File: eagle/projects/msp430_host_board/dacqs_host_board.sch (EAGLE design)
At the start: 114 parts, among them J1 MOL-SL-4-RA, J10 MOL-SL-3-V, J13 JST-PH-2TH-RA, J14 USB_MICROB_RECPT, J16 MOL-SL-2-RA, J17 CLM-112-02-L-D-IMU-MOUNT_IMU, J18 MOLSL-7-RA, J2 MOL-SL-4-RA, J3 MOL-SL-4-RA, J4 MOL-SL-4-RA, J5 MOL-SL-5-RA, J6 MOL-SL-3-V, J7 MOL-SL-5-V, J8 MOL-SL-3-RA, J9 MOL-SL-4-RA, U1 MSP430FR4994, U2 MSP430FR4994, U3 PCT2075D,118, U4 MS560702BA03-50, U5 TPS61240DRVR, U6 LP5907_DBV_5, U7 MCP73831T, U8 INA219AIDCNR, U9 STD12NF06LT4, Y1 32.768kHz, Y2 4MHz, Y3 32.768kHz, Y4 4MHz

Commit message: Bunch of small changes
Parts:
- added NC1, NC2, NC3, NC4: NC, daqcs_host:NO_CONNECT
- added TP1, TP10, TP11, TP12, TP13, TP14, TP15, TP16, TP17, TP18, TP19, TP2, TP20, TP21, TP22, TP23, TP24, TP25, TP26, TP27, TP28, TP29, TP3, TP30, TP31, TP32, TP33, TP34, TP4, TP5, TP6, TP7, TP8, TP9: (no value), daqcs_host:TEST_POINT_TP10R_SMD_10R_SMD
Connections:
- net N$47 renamed LED_BLUE_5V
- new net N$1: NC1.NC, R12.2
- new net N$2: NC3.NC, U$1.DAT1
- new net N$3: NC4.NC, U$1.DAT2
- net +5V: now also TP34.TP
- net ACT_CURRENT_IN: now also TP23.TP
- net ACT_SPEED_IN: now also TP22.TP
- net COMMS_MISO: now also TP15.TP
- net COMMS_MOSI: now also TP16.TP
- net COMMS_SCLK: now also TP14.TP
- net COMMS_SS: now also TP13.TP
- net CURRENT_PWM_OUT: now also TP19.TP
- net CUTDOWN_EN: now also TP17.TP
- net DIR_MOTOR_OUT: now also TP21.TP
- net EN_MOTOR_OUT: now also TP20.TP
- net IMU_MISO: now also TP30.TP
- net IMU_MOSI: now also TP33.TP
- net IMU_SCLK: now also TP32.TP
- net IMU_SS: now also TP31.TP
- net N$30: now also NC2.NC
- net RST_PI_1: now also TP3.TP
- net RST_PI_2: now also TP6.TP
- net RST_PI_3: now also TP9.TP
- net RST_PI_4: now also TP12.TP
- net SENSE_SCL_1: now also TP27.TP, TP29.TP
- net SENSE_SCL_2: now also TP25.TP
- net SENSE_SDA_1: now also TP26.TP, TP28.TP
- net SENSE_SDA_2: now also TP24.TP
- net SPEED_PWM_OUT: now also TP18.TP
- net UART_1_RX: now also TP2.TP
- net UART_1_TX: now also TP1.TP
- net UART_2_RX: now also TP5.TP
- net UART_2_TX: now also TP4.TP
- net UART_3_RX: now also TP8.TP
- net UART_3_TX: now also TP7.TP
- net UART_4_RX: now also TP11.TP
- net UART_4_TX: now also TP10.TP
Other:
- moved on the sheet: C27, J11

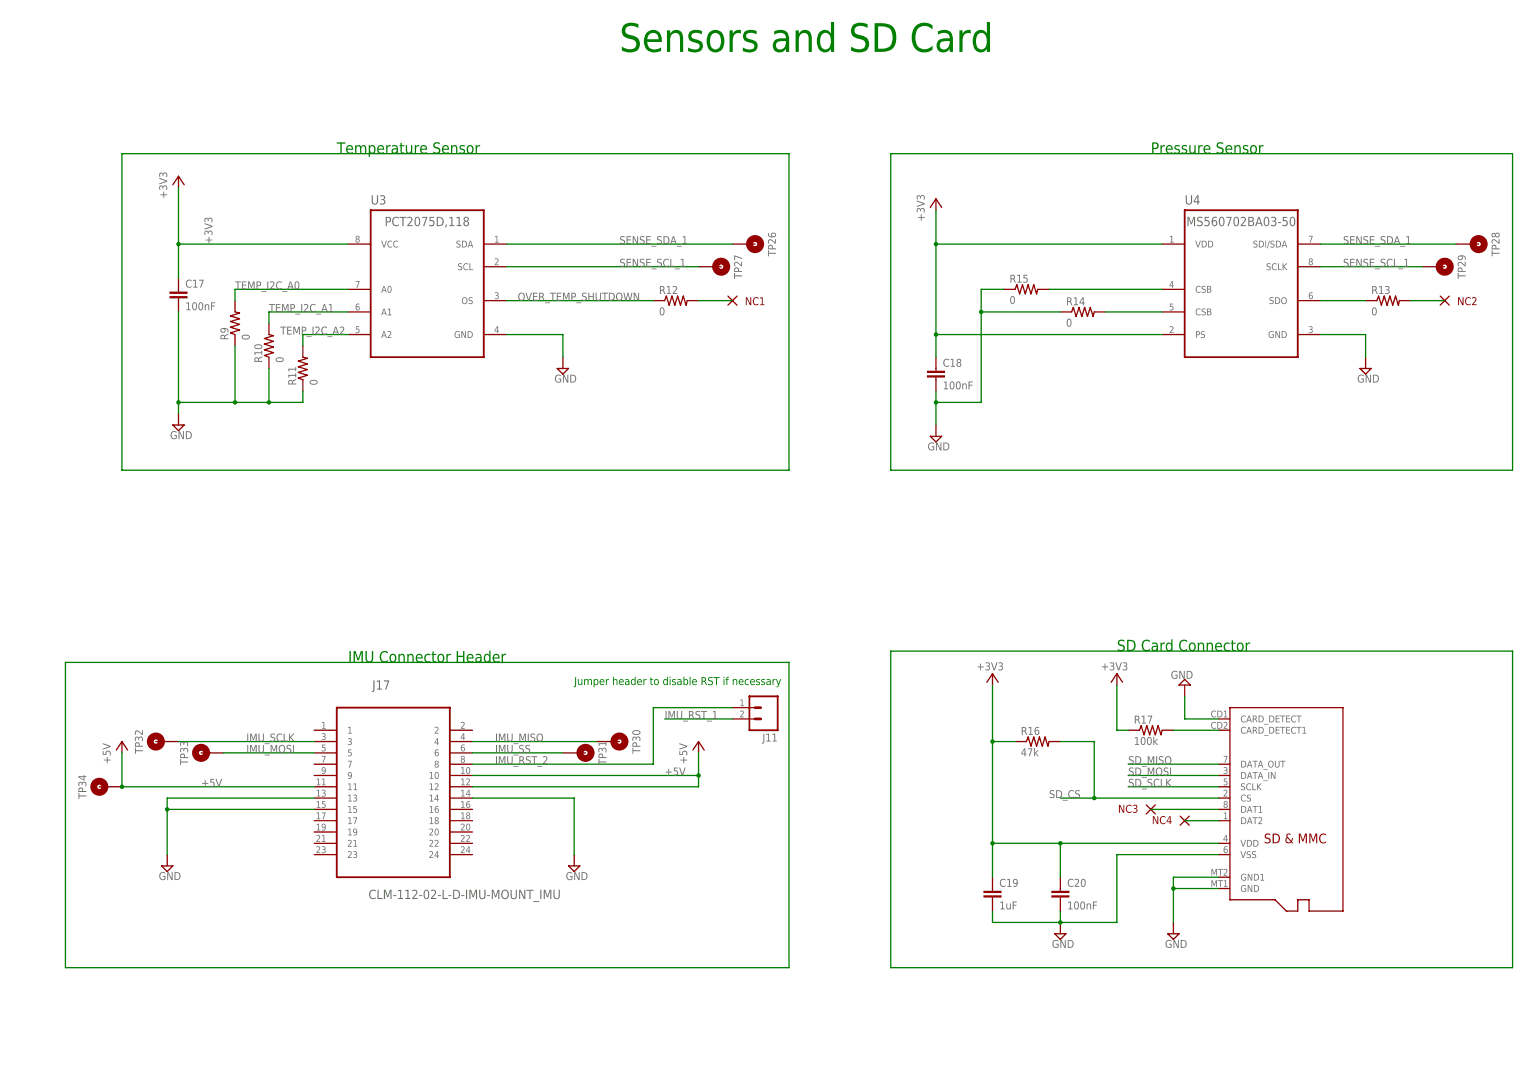
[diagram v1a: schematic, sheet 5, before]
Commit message: Added additional IMU with I2C interface
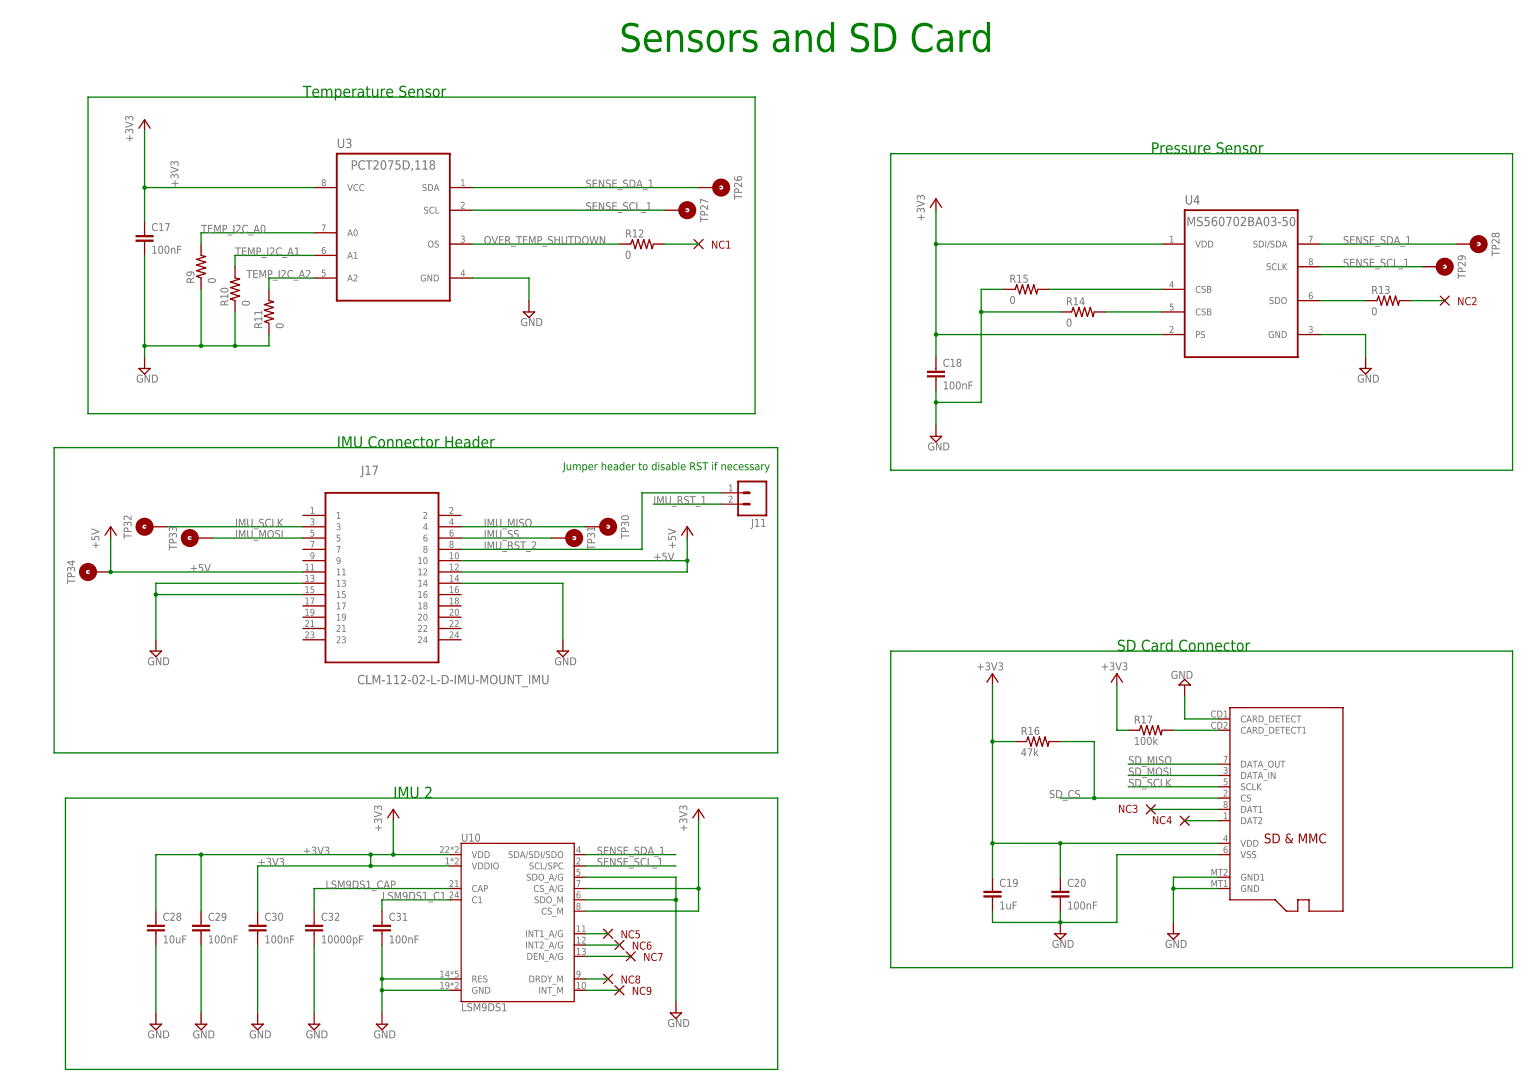
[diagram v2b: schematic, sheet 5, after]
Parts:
- added C28: 10uF, daqcs_host:CAP_10UF0_0603
- added C29, C30, C31: 100nF, daqcs_host:CAP_100NF0_0603
- added C32: 10000pF, daqcs_host:CAP_10000PF0_0603
- added NC5, NC6, NC7, NC8, NC9: NC, daqcs_host:NO_CONNECT
- added U10: LSM9DS1, daqcs_host:LSM9DS1
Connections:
- new net LSM9DS1_C1: C31.1, U10.C1
- new net LSM9DS1_CAP: C32.1, U10.CAP
- new net N$22: NC8.NC, U10.DRDY_M
- new net N$23: NC9.NC, U10.INT_M
- new net N$7: NC5.NC, U10.INT1_A/G
- new net N$8: NC6.NC, U10.INT2_A/G
- new net N$9: NC7.NC, U10.DEN_A/G
- net +3V3: now also C28.1, C29.1, C30.1, U10.CS_A/G, U10.CS_M, U10.VDD, U10.VDDIO
- net GND: now also C28.2, C29.2, C30.2, C31.2, C32.2, U10.GND, U10.RES, U10.SDO_A/G, U10.SDO_M
- net SENSE_SCL_1: now also U10.SCL/SPC
- net SENSE_SDA_1: now also U10.SDA/SDI/SDO
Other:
- note added: "IMU 2"
- moved on the sheet: C17, J11, J17, NC1, R10, R11, R12, R9, TP26, TP27, TP30, TP31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

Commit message: Added title page
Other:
- note added: "DATA ACQUISITION AND CONTROL HOST BOARD"
- note added: "HOST MSP430 CONNECTORS"
- note added: "HOST MSP430 SCHEMATIC"
- note added: "MAIN BOARD BLOCK DIAGRAM"
- note added: "MOTOR CONTROL MSP430 SCH"
- note added: "MOTOR CONTROL MSP430 SCHEMATIC"
- note added: "MOTOR MSP430 CONNECTORS"
- note added: "POWER MANAGEMENT SCHEMATIC"
- note added: "REACTION WHEEL BATTERY VOLTAGE SENSE"
- note added: "REACTION WHEEL BATTERY VOLTAGE SENSE SCHEMATIC"
- note added: "RW BATTERY VOLTAGE SENSE"
- note added: "SENSORS AND SD CARD SCHEMATIC"
- note added: "SENSORS AND SD CARD SCHEMATICS"
- note added: "TABLE OF CONTENTS"

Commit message: fixed some ERC errors and warnings
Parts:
- added TP35, TP36, TP37, TP38: (no value), daqcs_host:TEST_POINT_TP10R_SMD_10R_SMD
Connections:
- removed net AVCC: C1.1
- removed net IMU_RST: U2.P2.7
- removed net N$34: R17.2, U$1.CARD_DETECT1
- removed net SD_SS: U2.P5.7_UCA2STE_TA4.1_MCLK
- removed net VBAT_POS_RETURN: J16.2
- removed net VBAT_SENSE_P: J15.2, R22.1, U8.VIN+
- new net N$6: J16.2, U9.P$2
- net +3V3: now also TP37.TP, U6.VOUT_3V3; no longer U6.VOUT
- net +5V: now also TP36.TP, U5.VOUT_5V; no longer U5.VOUT
- net AVCC_HOST: now also C1.1
- net BATT_CHARGE_STAT: now also TP38.TP
- net CUTDOWN_EN: now also U9.P$1; no longer U9.1
- net GND: now also BAT1.V-, U9.P$3
- net IMU_RST_1: now also U2.P2.7
- net SD_CS: now also U2.P5.7_UCA2STE_TA4.1_MCLK
- net SD_DETECT: now also R17.2, U$1.CARD_DETECT1
- net VBAT: now also J15.2, R22.1, U8.VIN+
- net VBAT_SENSE_N: now also TP35.TP
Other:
- note added: "Accelerometer/Gyro R/W = 11010101/11010100"
- note added: "I2C Address: 1001000"
- note added: "I2C Address: 11101111"
- note added: "I2C Slave Address: 1000000"
- note added: "Magnometer R/W = 00111001/00111000"
